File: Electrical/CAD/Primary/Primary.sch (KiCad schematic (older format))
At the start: 15 parts, among them Q1 2N3904, Q2 2N3906, SW1 SW_DPST, U1 LMC555xN, U2 MCP6282

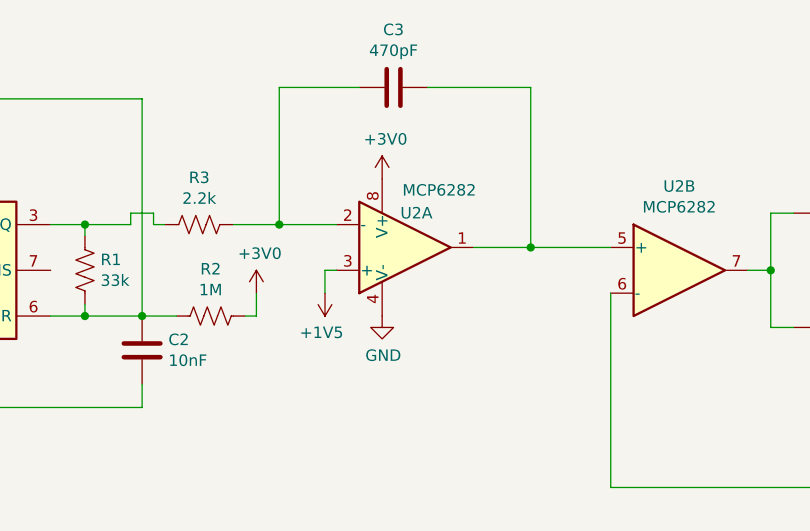
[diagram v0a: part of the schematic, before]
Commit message: Modified footprints for caps and battery on primary PCB.
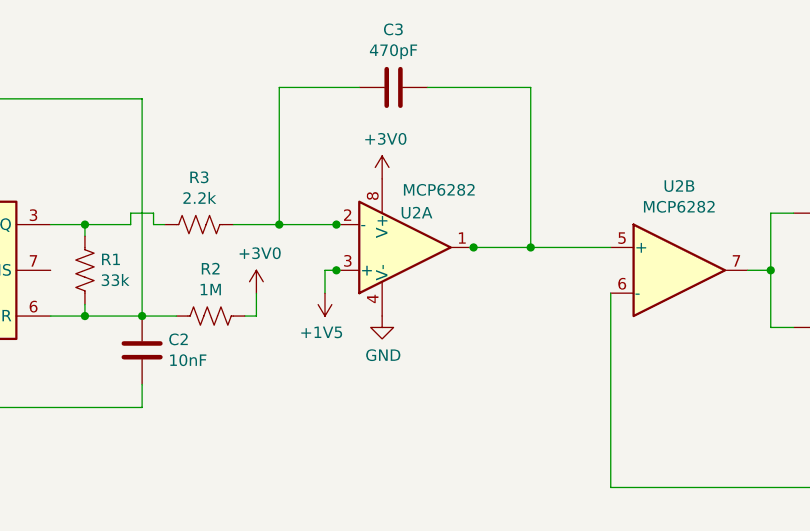
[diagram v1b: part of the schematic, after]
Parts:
- C1, C2, C3, C4: footprint Capacitor_THT:CP_Radial_D6.3mm_P2.50mm -> Capacitor_THT:C_Disc_D6.0mm_W2.5mm_P5.00mm
- L1: footprint Jumper:SolderJumper-2_P1.3mm_Open_Pad1.0x1.5mm -> WirelessPower:CoilSpiral_25_Bezier
